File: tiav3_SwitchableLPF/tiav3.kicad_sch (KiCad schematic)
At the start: 37 parts, among them J1 SSQ-103-01-G-D, J2 Conn_Coaxial, J3 SSQ-102-01-G-D, U1 OPA847IDBVT, U2 OPA842xDBV, U3 TMUX1209RSVR

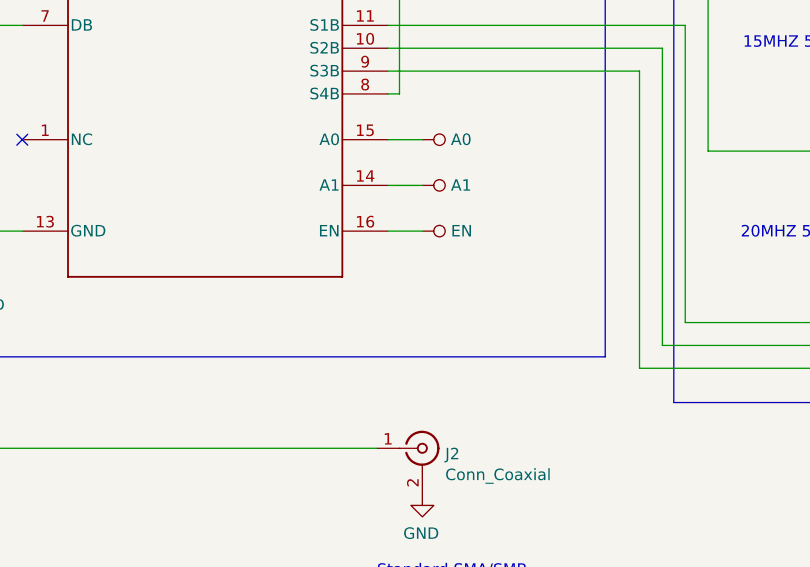
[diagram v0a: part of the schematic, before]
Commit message: Performed claude analysis on the project and fixed risk 4
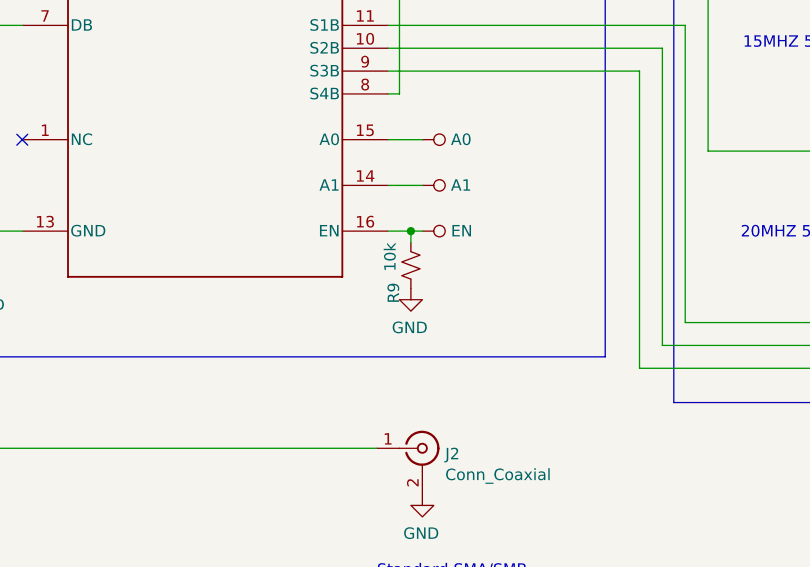
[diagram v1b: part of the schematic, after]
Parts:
- added R9: 10k, Resistor_SMD:R_0402_1005Metric_Pad0.72x0.64mm_HandSolder, symbol Device:R_Small_US
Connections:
- net EN: now also R9.2
- net GND: now also R9.1
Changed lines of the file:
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@@
 	)
 	(junction
+		(at 289.56 198.12)
+		(diameter 0)
+		(color 0 0 0 0)
+	)
+	(junction
 		(at 360.68 142.24)
 		(diameter 0)
@@
 	(wire
 		(pts
+			(xy 289.56 199.39) (xy 289.56 198.12)
+		)
+		(stroke
+			(width 0)
+			(type default)
+		)
+	)
+	(wire
+		(pts
 			(xy 152.4 157.48) (xy 114.3 157.48)
 		)
@@
 	(wire
 		(pts
+			(xy 289.56 198.12) (xy 290.83 198.12)
+		)
+		(stroke
+			(width 0)
+			(type default)
+		)
+	)
+	(wire
+		(pts
 			(xy 317.5 210.82) (xy 317.5 177.8)
 		)
@@
 	(wire
 		(pts
-			(xy 287.02 198.12) (xy 290.83 198.12)
+			(xy 287.02 198.12) (xy 289.56 198.12)
 		)
 		(stroke
@@
 	)
 	(symbol
+		(lib_id "power:GND")
+		(at 289.56 204.47 0)
+		(mirror y)
+		(unit 1)
+		(exclude_from_sim no)
+		(in_bom yes)
+		(on_board yes)
+		(dnp no)
+		(property "Reference" "#PWR013"
+			(at 289.56 210.82 0)
+			(effects
+				(font
+					(size 1.27 1.27)
+				)
+				(hide yes)
+			)
+		)
+		(property "Value" "GND"
+			(at 289.433 208.8642 0)
+			(effects
+				(font
+					(size 1.27 1.27)
+				)
+			)
+		)
+		(property "Footprint" ""
+			(at 289.56 204.47 0)
+			(effects
+				(font
+					(size 1.27 1.27)
+				)
+				(hide yes)
+			)
+		)
+		(property "Datasheet" ""
+			(at 289.56 204.47 0)
+			(effects
+				(font
+					(size 1.27 1.27)
+				)
+				(hide yes)
+			)
+		)
+		(property "Description" ""
+			(at 289.56 204.47 0)
+			(effects
+				(font
+					(size 1.27 1.27)
+				)
+			)
+		)
+		(pin "1"
+		)
+		(instances
+			(project "tiav3"
+				(path "/548ba79d-aa60-452e-83bc-59e3672545ef"
+					(reference "#PWR013")
+					(unit 1)
+				)
+			)
+		)
+	)
+	(symbol
 		(lib_id "Device:R_Small_US")
 		(at 226.06 143.51 270)
@@
 					(unit 1)
 				)
+			)
+		)
+	)
+	(symbol
+		(lib_id "Device:R_Small_US")
+		(at 289.56 201.93 180)
+		(unit 1)
+		(exclude_from_sim no)
+		(in_bom yes)
+		(on_board yes)
+		(dnp no)
+		(property "Reference" "R9"
+			(at 287.655 203.835 90)
+			(effects
+				(font
+					(size 1.27 1.27)
+				)
+				(justify left)
+			)
+		)
+		(property "Value" "10k"
+			(at 287.274 199.39 90)
+			(effects
+				(font
+					(size 1.27 1.27)
+				)
+				(justify left)
+			)
+		)
+		(property "Footprint" "Resistor_SMD:R_0402_1005Metric_Pad0.72x0.64mm_HandSolder"
+			(at 289.56 201.93 0)
+			(effects
+				(font
+					(size 1.27 1.27)
+				)
+				(hide yes)
+			)
+		)
+		(property "Datasheet" "~"
+			(at 289.56 201.93 0)
+			(effects
+				(font
+					(size 1.27 1.27)
+				)
+				(hide yes)
+			)
+		)
+		(property "Description" ""
+			(at 289.56 201.93 0)
+			(effects
+				(font
+					(size 1.27 1.27)
+				)
+			)
+		)
+		(pin "1"
+		)
+		(pin "2"
+		)
+		(instances
+			(project "tiav3"
+				(path "/548ba79d-aa60-452e-83bc-59e3672545ef"
+					(reference "R9")
+					(unit 1)
+				)

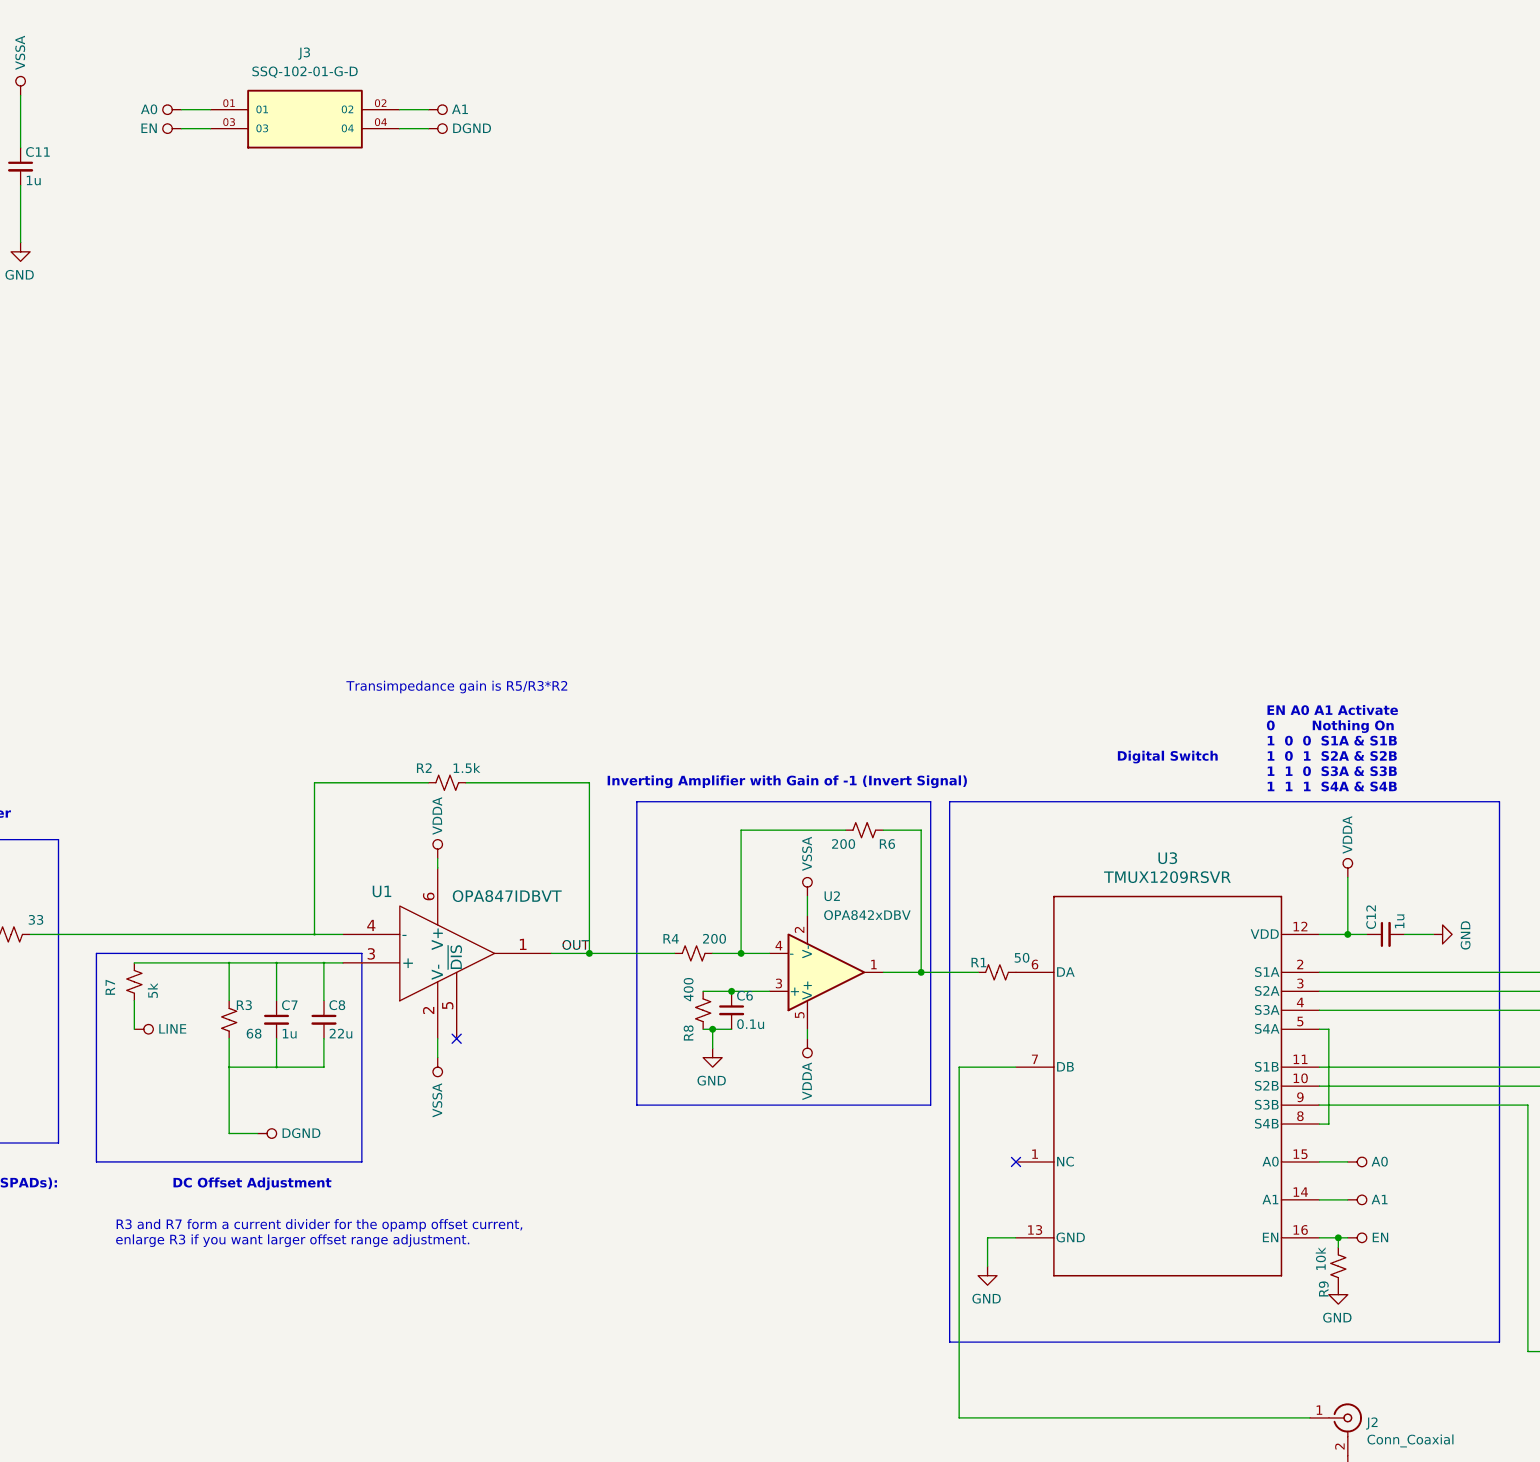
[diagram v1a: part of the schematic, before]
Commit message: Created the 50 ohm impedance and changed EN pin to Ground
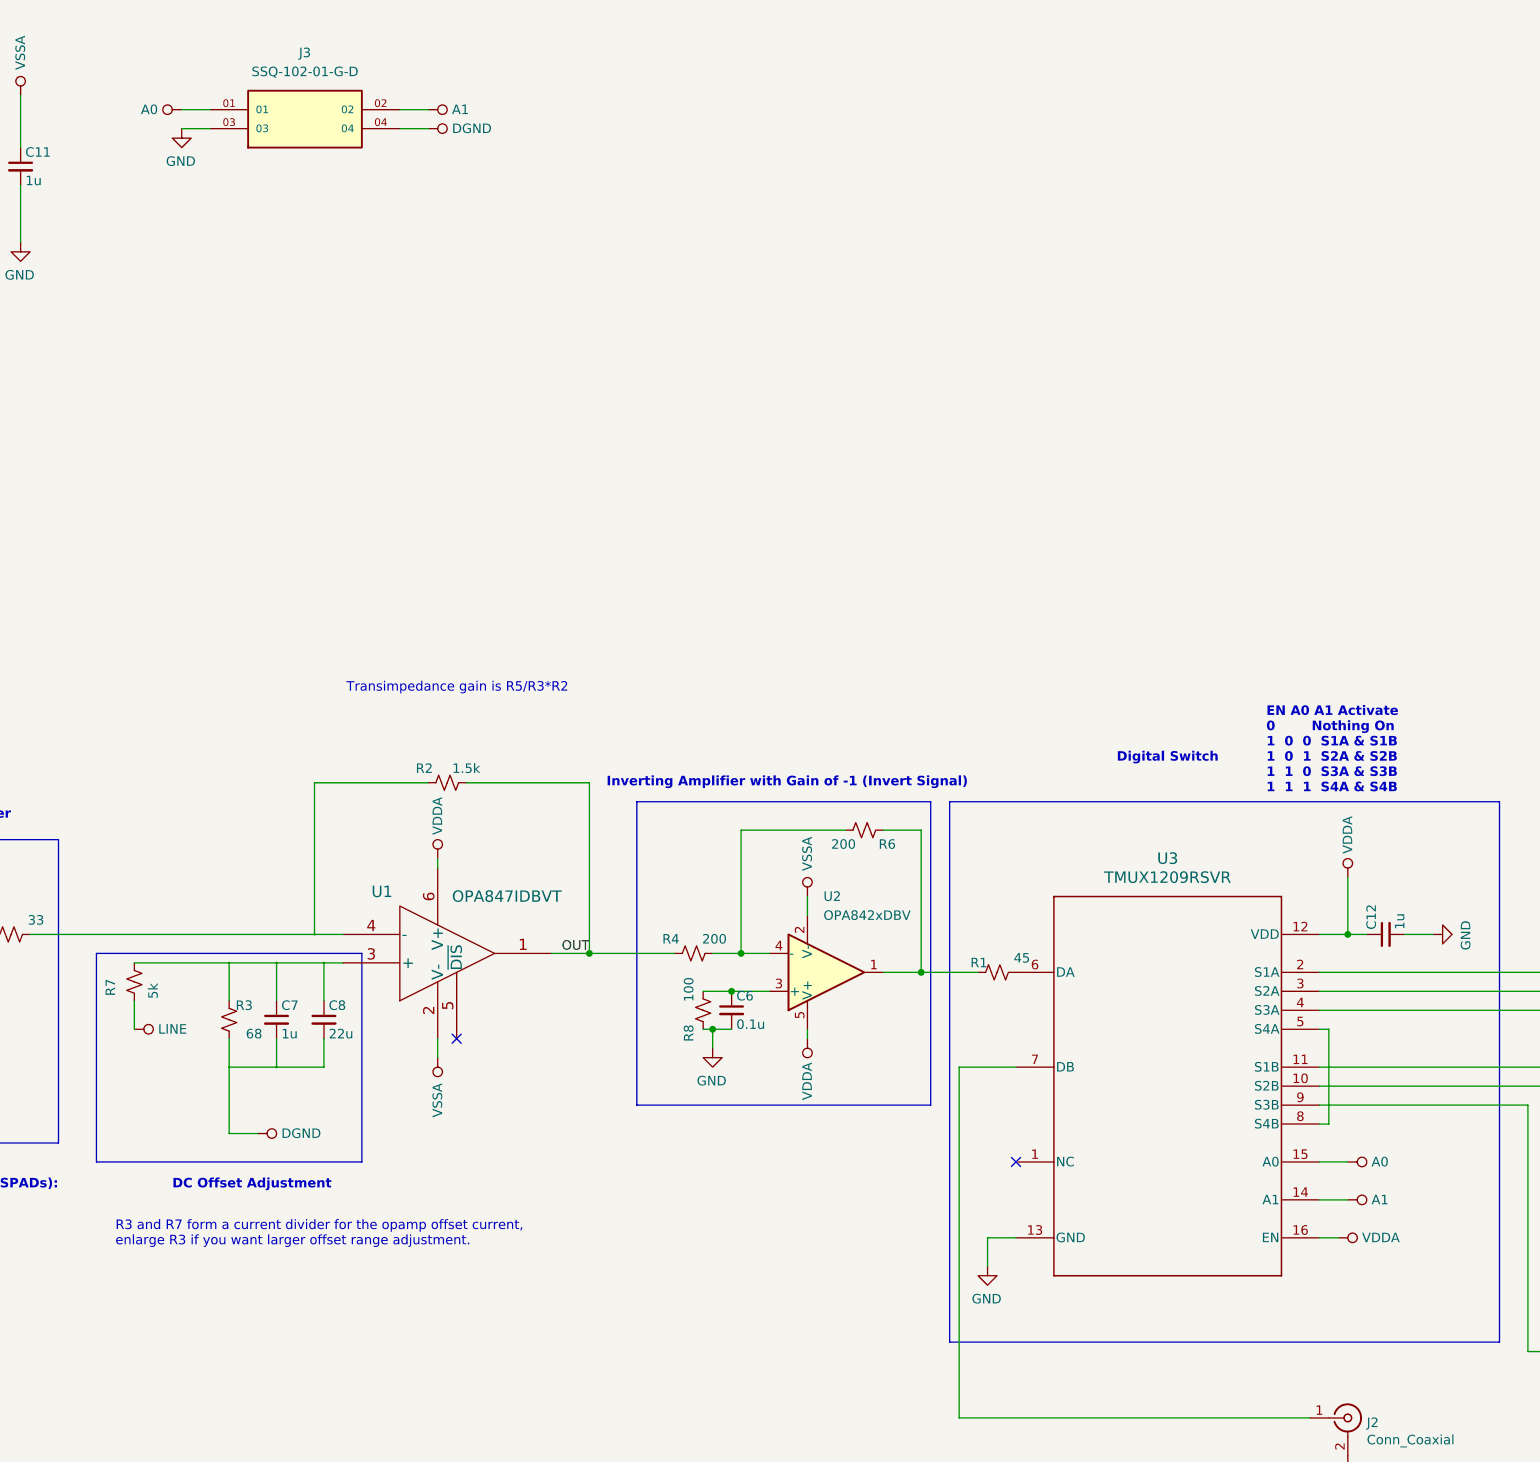
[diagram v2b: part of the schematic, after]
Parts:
- removed R9: 10k, Resistor_SMD:R_0402_1005Metric_Pad0.72x0.64mm_HandSolder, symbol Device:R_Small_US
- R1: value 50 -> 45
- R8: value 400 -> 100
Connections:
- net GND: now also J3.03
- net VDDA: now also U3.16 (EN)
- removed net EN: J3.03, U3.16 (EN)
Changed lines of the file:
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@@
 	)
 	(junction
-		(at 289.56 198.12)
-		(diameter 0)
-		(color 0 0 0 0)
-	)
-	(junction
 		(at 360.68 142.24)
 		(diameter 0)
@@
 	(wire
 		(pts
-			(xy 289.56 199.39) (xy 289.56 198.12)
-		)
-		(stroke
-			(width 0)
-			(type default)
-		)
-	)
-	(wire
-		(pts
 			(xy 152.4 157.48) (xy 114.3 157.48)
 		)
@@
 	(wire
 		(pts
+			(xy 287.02 198.12) (xy 289.56 198.12)
+		)
+		(stroke
+			(width 0)
+			(type default)
+		)
+	)
+	(wire
+		(pts
 			(xy 152.4 157.48) (xy 156.21 157.48)
 		)
@@
 	(wire
 		(pts
-			(xy 289.56 198.12) (xy 290.83 198.12)
-		)
-		(stroke
-			(width 0)
-			(type default)
-		)
-	)
-	(wire
-		(pts
 			(xy 317.5 210.82) (xy 317.5 177.8)
 		)
@@
 	(wire
 		(pts
-			(xy 287.02 198.12) (xy 289.56 198.12)
-		)
-		(stroke
-			(width 0)
-			(type default)
-		)
-	)
-	(wire
-		(pts
 			(xy 379.73 189.23) (xy 379.73 213.36)
 		)
@@
 			)
 		)
-		(property "Value" "50"
+		(property "Value" "45"
 			(at 248.285 160.655 90)
 			(effects
@@
 	)
 	(symbol
-		(lib_id "power:VDDA")
-		(at 290.83 198.12 270)
-		(mirror x)
-		(unit 1)
-		(exclude_from_sim no)
-		(in_bom yes)
-		(on_board yes)
-		(dnp no)
-		(property "Reference" "#PWR033"
-			(at 287.02 198.12 0)
-			(effects
-				(font
-					(size 1.27 1.27)
-				)
-				(hide yes)
-			)
-		)
-		(property "Value" "EN"
-			(at 294.005 198.12 90)
-			(effects
-				(font
-					(size 1.27 1.27)
-				)
-				(justify left)
-			)
-		)
-		(property "Footprint" ""
-			(at 290.83 198.12 0)
-			(effects
-				(font
-					(size 1.27 1.27)
-				)
-				(hide yes)
-			)
-		)
-		(property "Datasheet" ""
-			(at 290.83 198.12 0)
-			(effects
-				(font
-					(size 1.27 1.27)
-				)
-				(hide yes)
-			)
-		)
-		(property "Description" ""
-			(at 290.83 198.12 0)
-			(effects
-				(font
-					(size 1.27 1.27)
-				)
-			)
-		)
-		(pin "1"
-		)
-		(instances
-			(project "tiav3"
-				(path "/548ba79d-aa60-452e-83bc-59e3672545ef"
-					(reference "#PWR033")
-					(unit 1)
-				)
-			)
-		)
-	)
-	(symbol
 		(lib_id "Device:L_Small")
 		(at 352.552 142.24 90)
@@
 	)
 	(symbol
-		(lib_id "power:VDDA")
-		(at 134.62 49.53 90)
-		(unit 1)
-		(exclude_from_sim no)
-		(in_bom yes)
-		(on_board yes)
-		(dnp no)
-		(property "Reference" "#PWR036"
-			(at 138.43 49.53 0)
-			(effects
-				(font
-					(size 1.27 1.27)
-				)
-				(hide yes)
-			)
-		)
-		(property "Value" "EN"
-			(at 131.445 49.53 90)
-			(effects
-				(font
-					(size 1.27 1.27)
-				)
-				(justify left)
-			)
-		)
-		(property "Footprint" ""
-			(at 134.62 49.53 0)
-			(effects
-				(font
-					(size 1.27 1.27)
-				)
-				(hide yes)
-			)
-		)
-		(property "Datasheet" ""
-			(at 134.62 49.53 0)
-			(effects
-				(font
-					(size 1.27 1.27)
-				)
-				(hide yes)
-			)
-		)
-		(property "Description" ""
-			(at 134.62 49.53 0)
-			(effects
-				(font
-					(size 1.27 1.27)
-				)
-			)
-		)
-		(pin "1"
-		)
-		(instances
-			(project "tiav3"
-				(path "/548ba79d-aa60-452e-83bc-59e3672545ef"
-					(reference "#PWR036")
-					(unit 1)
-				)
-			)
-		)
-	)
-	(symbol
 		(lib_id "Device:C_Small")
 		(at 105.41 54.61 0)
@@
 	)
 	(symbol
-		(lib_id "power:GND")
-		(at 289.56 204.47 0)
-		(mirror y)
-		(unit 1)
-		(exclude_from_sim no)
-		(in_bom yes)
-		(on_board yes)
-		(dnp no)
-		(property "Reference" "#PWR013"
-			(at 289.56 210.82 0)
-			(effects
-				(font
-					(size 1.27 1.27)
-				)
-				(hide yes)
-			)
-		)
-		(property "Value" "GND"
-			(at 289.433 208.8642 0)
-			(effects
-				(font
-					(size 1.27 1.27)
-				)
-			)
-		)
-		(property "Footprint" ""
-			(at 289.56 204.47 0)
-			(effects
-				(font
-					(size 1.27 1.27)
-				)
-				(hide yes)
-			)
-		)
-		(property "Datasheet" ""
-			(at 289.56 204.47 0)
-			(effects
-				(font
-					(size 1.27 1.27)
-				)
-				(hide yes)
-			)
-		)
-		(property "Description" ""
-			(at 289.56 204.47 0)
-			(effects
-				(font
-					(size 1.27 1.27)
-				)
-			)
-		)
-		(pin "1"
-		)
-		(instances
-			(project "tiav3"
-				(path "/548ba79d-aa60-452e-83bc-59e3672545ef"
-					(reference "#PWR013")
-					(unit 1)
-				)
-			)
-		)
-	)
-	(symbol
 		(lib_id "Device:R_Small_US")
 		(at 226.06 143.51 270)
@@
 			)
 		)
-		(property "Value" "400"
+		(property "Value" "100"
 			(at 202.565 163.195 90)
 			(effects
@@
 	)
 	(symbol
-		(lib_id "Device:R_Small_US")
-		(at 289.56 201.93 180)
+		(lib_id "power:GND")
+		(at 360.172 199.39 0)
+		(mirror y)
 		(unit 1)
 		(exclude_from_sim no)
@@
 		(on_board yes)
 		(dnp no)
-		(property "Reference" "R9"
-			(at 287.655 203.835 90)
+		(property "Reference" "#PWR029"
+			(at 360.172 205.74 0)
 			(effects
 				(font
 					(size 1.27 1.27)
 				)
-				(justify left)
+				(hide yes)
 			)
 		)
-		(property "Value" "10k"
-			(at 287.274 199.39 90)
+		(property "Value" "GND"
+			(at 360.045 203.7842 0)
 			(effects
 				(font
 					(size 1.27 1.27)
 				)
-				(justify left)
 			)
 		)
-		(property "Footprint" "Resistor_SMD:R_0402_1005Metric_Pad0.72x0.64mm_HandSolder"
-			(at 289.56 201.93 0)
+		(property "Footprint" ""
+			(at 360.172 199.39 0)
 			(effects
 				(font
@@
 			)
 		)
-		(property "Datasheet" "~"
-			(at 289.56 201.93 0)
+		(property "Datasheet" ""
+			(at 360.172 199.39 0)
 			(effects
 				(font
@@
 		)
 		(property "Description" ""
-			(at 289.56 201.93 0)
+			(at 360.172 199.39 0)
 			(effects
 				(font
@@
 		(pin "1"
 		)
-		(pin "2"
-		)
 		(instances
 			(project "tiav3"
 				(path "/548ba79d-aa60-452e-83bc-59e3672545ef"
-					(reference "R9")
+					(reference "#PWR029")
 					(unit 1)
 				)
@@
 	(symbol
 		(lib_id "power:GND")
-		(at 360.172 199.39 0)
+		(at 134.62 49.53 0)
 		(mirror y)
 		(unit 1)
@@
 		(on_board yes)
 		(dnp no)
-		(property "Reference" "#PWR029"
-			(at 360.172 205.74 0)
+		(property "Reference" "#PWR033"
+			(at 134.62 55.88 0)
 			(effects
 				(font
@@
 		)
 		(property "Value" "GND"
-			(at 360.045 203.7842 0)
+			(at 134.493 53.9242 0)
 			(effects
 				(font
@@
 		)
 		(property "Footprint" ""
-			(at 360.172 199.39 0)
+			(at 134.62 49.53 0)
 			(effects
 				(font
@@
 		)
 		(property "Datasheet" ""
-			(at 360.172 199.39 0)
+			(at 134.62 49.53 0)
 			(effects
 				(font
@@
 		)
 		(property "Description" ""
-			(at 360.172 199.39 0)
+			(at 134.62 49.53 0)
 			(effects
 				(font
@@
 			(project "tiav3"
 				(path "/548ba79d-aa60-452e-83bc-59e3672545ef"
-					(reference "#PWR029")
+					(reference "#PWR033")
 					(unit 1)
 				)
@@
 					(unit 1)
 				)
+			)
+		)
+	)
+	(symbol
+		(lib_id "power:VDDA")
+		(at 289.56 198.12 270)
+		(mirror x)
+		(unit 1)
+		(exclude_from_sim no)
+		(in_bom yes)
+		(on_board yes)
+		(dnp no)
+		(property "Reference" "#PWR013"
+			(at 285.75 198.12 0)
+			(effects
+				(font
+					(size 1.27 1.27)
+				)
+				(hide yes)
+			)
+		)
+		(property "Value" "VDDA"
+			(at 292.735 198.12 90)
+			(effects
+				(font
+					(size 1.27 1.27)
+				)
+				(justify left)
+			)
+		)
+		(property "Footprint" ""
+			(at 289.56 198.12 0)
+			(effects
+				(font
+					(size 1.27 1.27)
+				)
+				(hide yes)
+			)
+		)
+		(property "Datasheet" ""
+			(at 289.56 198.12 0)
+			(effects
+				(font
+					(size 1.27 1.27)
+				)
+				(hide yes)
+			)
+		)
+		(property "Description" ""
+			(at 289.56 198.12 0)
+			(effects
+				(font
+					(size 1.27 1.27)
+				)
+			)
+		)
+		(pin "1"
+		)
+		(instances
+			(project "tiav3"
+				(path "/548ba79d-aa60-452e-83bc-59e3672545ef"
+					(reference "#PWR013")
+					(unit 1)
+				)
